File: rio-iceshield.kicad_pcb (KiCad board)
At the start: 2 copper layers, 87.6 x 56 mm, 71 parts, among them J2 Conn_01x06, J3 Conn_01x06, J4 Conn_01x06, J5 Conn_01x06, J6 Conn_01x06, J7 Conn_02x06_Odd_Even, U1 ICE40UP5K-SG48ITR, U10 PC817, U11 PC817, U12 PC817, U13 PC817, U14 PC817, U2 AT25SF081-SSHF-X, U3 LD3985M122R_SOT23, U4 ULN2803A, U5 ULN2803A, U7 PC817, U8 PC817, U9 PC817, X2 XO91, j1 GPIO

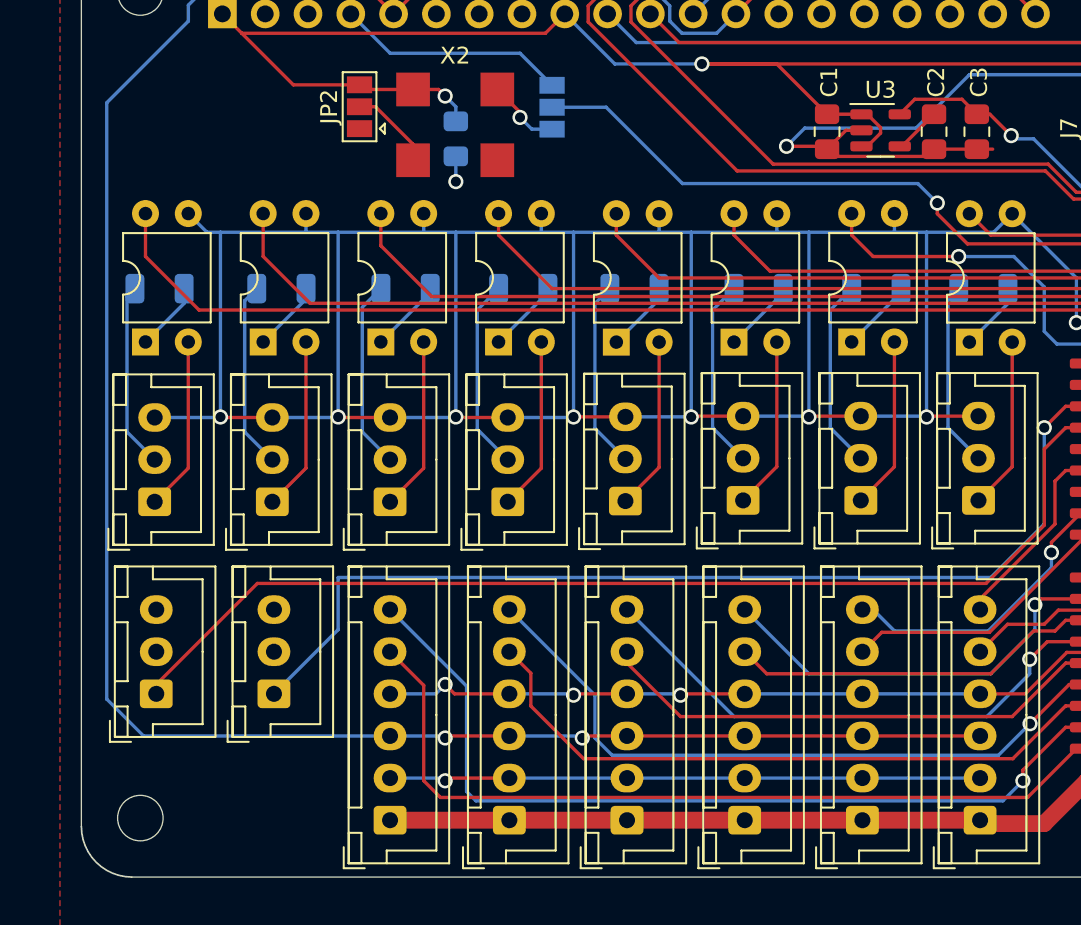
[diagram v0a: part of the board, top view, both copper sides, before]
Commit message: adding missing in/out powerlines
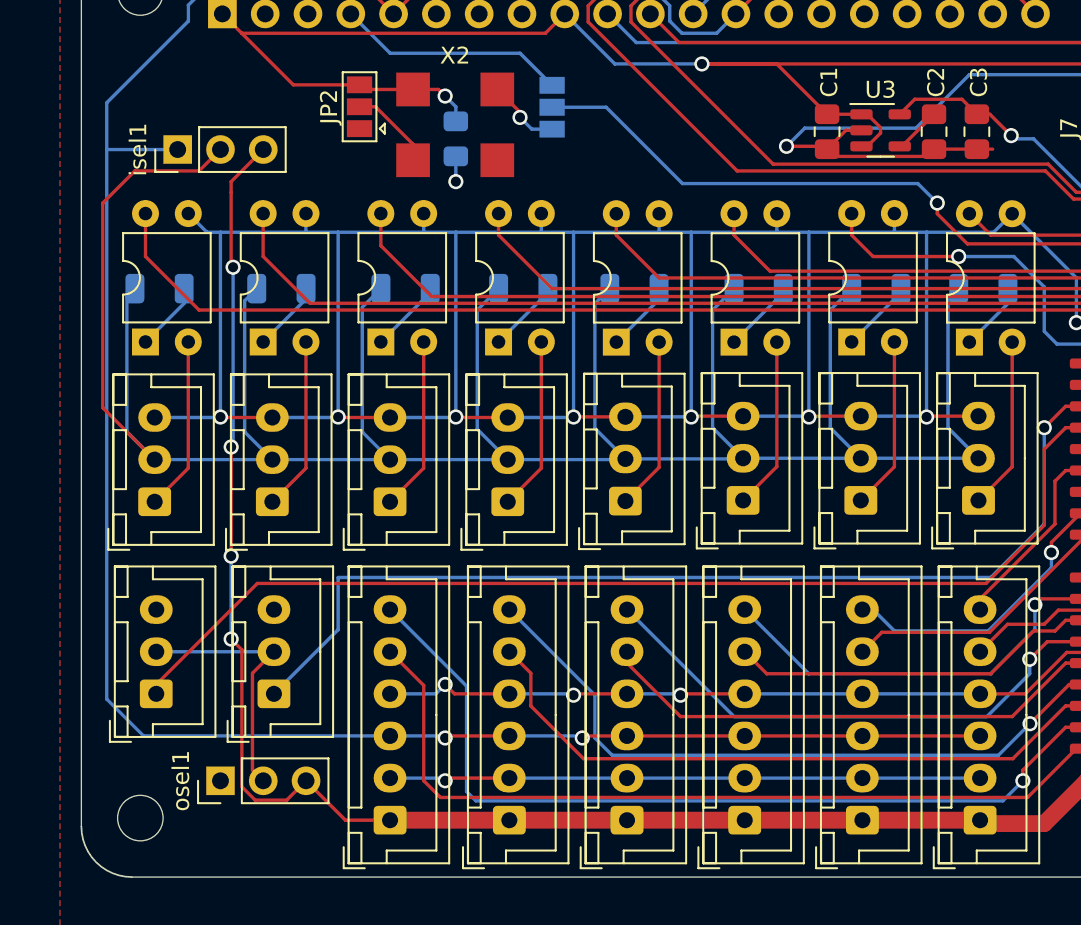
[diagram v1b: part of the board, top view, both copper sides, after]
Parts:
- added isel1: 5V 24V, Connector_PinHeader_2.54mm:PinHeader_1x03_P2.54mm_Vertical, F.Cu at (105.7, 56.8)
- added osel1: 5V 24V, Connector_PinHeader_2.54mm:PinHeader_1x03_P2.54mm_Vertical, F.Cu at (108.3, 94.3)
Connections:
- R2 pad 2: /input1/power -> in_power
- R3 pad 2: /input2/power -> in_power
- R4 pad 2: /input3/power -> in_power
- R5 pad 2: /input4/power -> in_power
- R6 pad 2: /input5/power -> in_power
- R7 pad 2: /input6/power -> in_power
- R8 pad 2: /input7/power -> in_power
- R9 pad 2: /input8/power -> in_power
- input1 pad 2: /input1/power -> in_power
- input2 pad 2: /input2/power -> in_power
- input3 pad 2: /input3/power -> in_power
- input4 pad 2: /input4/power -> in_power
- input5 pad 2: /input5/power -> in_power
- input6 pad 2: /input6/power -> in_power
- input7 pad 2: /input7/power -> in_power
- input8 pad 2: /input8/power -> in_power
- output1 pad 2: unconnected-(output1-Pin_2-Pad2) -> out_power
- output1 pad 3: unconnected-(output1-Pin_3-Pad3) -> gnd
- output2 pad 2: unconnected-(output2-Pin_2-Pad2) -> out_power
- output2 pad 3: unconnected-(output2-Pin_3-Pad3) -> gnd
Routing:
- net in_power: track 0.00 -> 163.6 mm
- net 12v: track 58.3 -> 108.1 mm, vias 0 -> 4
- net out_power: track 0.00 -> 15.4 mm
- net /input4/power: track 11.4 -> 0.00 mm
- net /input7/power: track 11.3 -> 0.00 mm
- net /input6/power: track 11.3 -> 0.00 mm
- net /input3/power: track 11.3 -> 0.00 mm
- net /input5/power: track 11.2 -> 0.00 mm
- net /input2/power: track 11.1 -> 0.00 mm
- net /input8/power: track 11.1 -> 0.00 mm
- net /input1/power: track 11.0 -> 0.00 mm
- net 5v: track 101.5 -> 105.7 mm

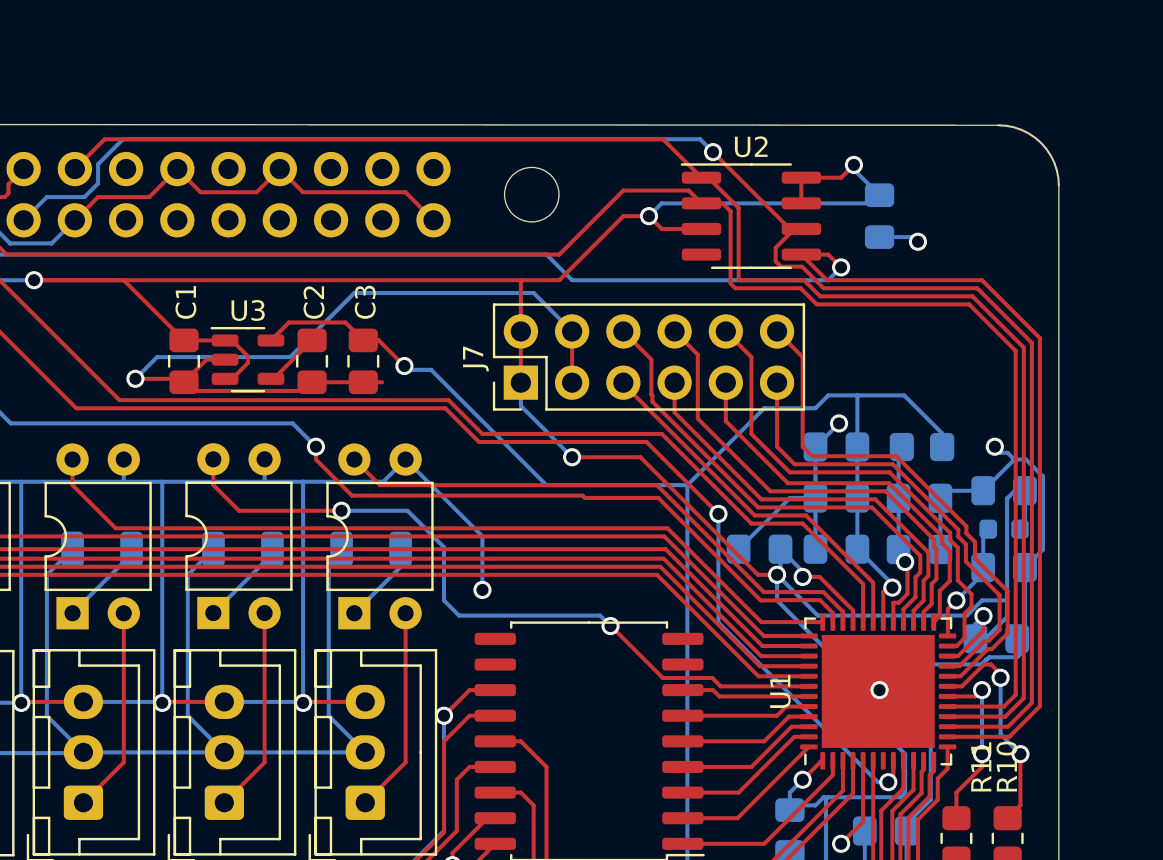
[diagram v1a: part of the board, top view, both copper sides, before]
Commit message: replacing spi-flash package
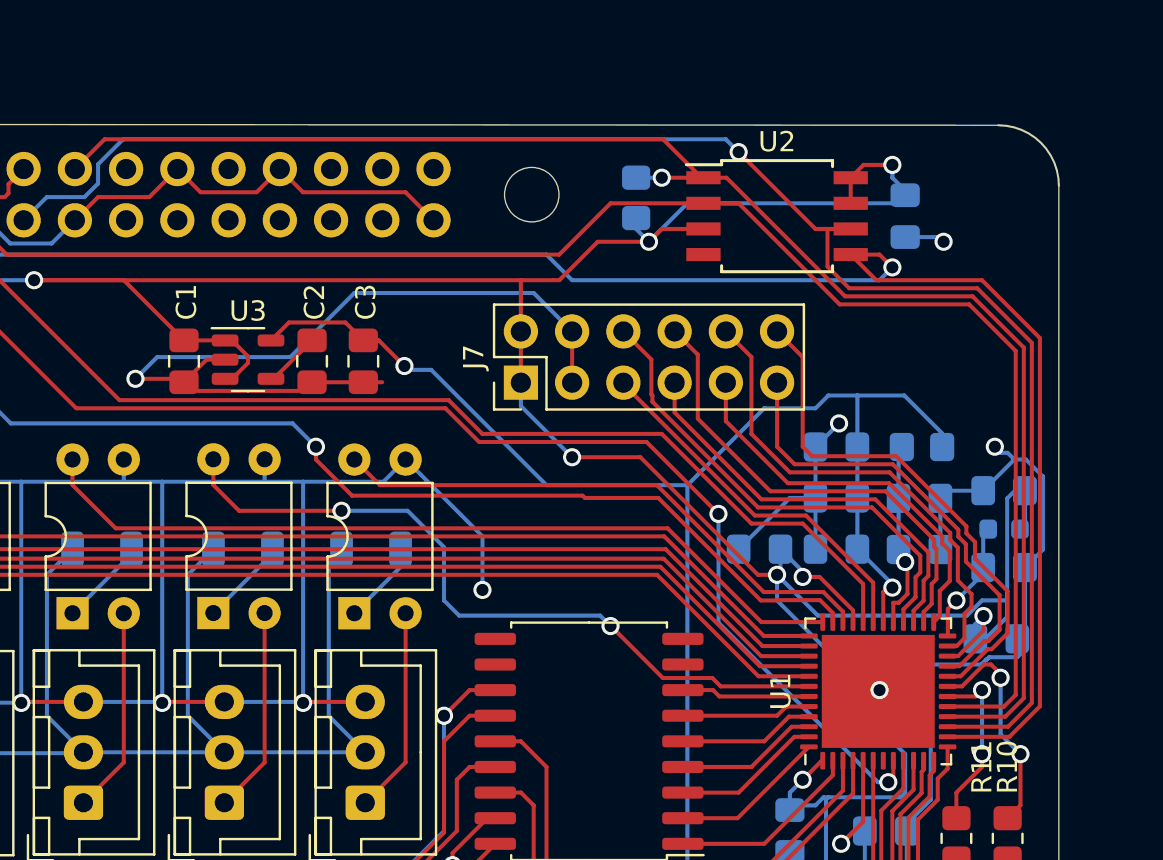
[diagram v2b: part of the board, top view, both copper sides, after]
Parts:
- added R12: 10k, Resistor_SMD:R_0805_2012Metric_Pad1.20x1.40mm_HandSolder, B.Cu at (166.7, 47.7)
- D1: value CDBU40-HF -> CDBU40-HF 800mV
- U2: value AT25SF081-SSHF-X -> AT25SF041B-SHD 4 Mb; footprint Package_SO:SOIC-8_3.9x4.9mm_P1.27mm -> Package_SO:SOIC-8W_5.3x5.3mm_P1.27mm
- isel1, osel1: value 5V 24V -> Conn_01x03
- moved U2 1.27 mm to (173.7, 48.6)
- moved C4 1.27 mm to (180.0, 48.6)
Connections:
- net Net-(D1-K) renamed 2v5
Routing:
- net SPI_MISO: track 79.8 -> 77.2 mm
- net 3v3: track 211.4 -> 213.3 mm
- net SPI_CS1: track 75.6 -> 76.7 mm, vias 0 -> 1
- net SPI_SCK: track 81.8 -> 81.2 mm

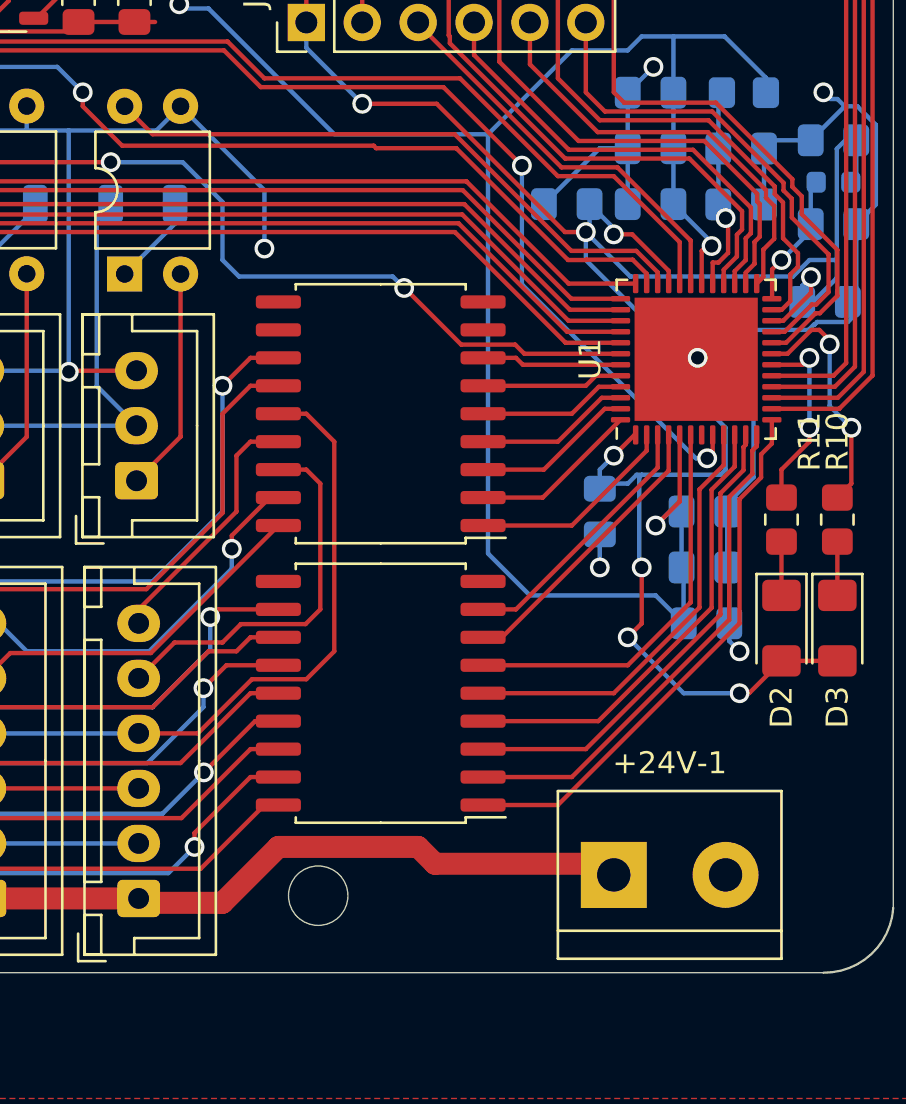
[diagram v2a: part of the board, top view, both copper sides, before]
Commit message: adding pulldowns to outputs / fixing uln gnd's
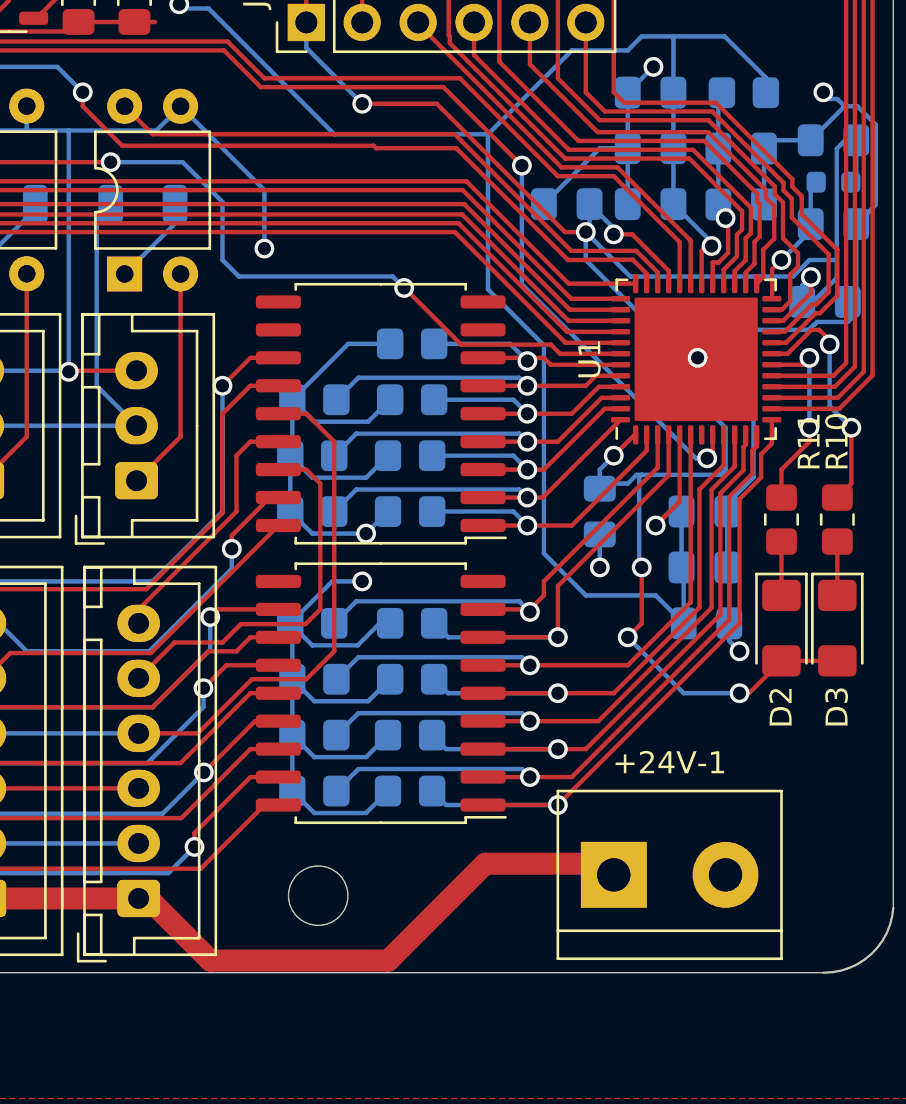
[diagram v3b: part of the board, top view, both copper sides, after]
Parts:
- added R13: 20k, Resistor_SMD:R_0805_2012Metric_Pad1.20x1.40mm_HandSolder, B.Cu at (165.7, 91.7)
- added R14: 20k, Resistor_SMD:R_0805_2012Metric_Pad1.20x1.40mm_HandSolder, B.Cu at (161.3, 91.7)
- added R15: 20k, Resistor_SMD:R_0805_2012Metric_Pad1.20x1.40mm_HandSolder, B.Cu at (165.7, 89.2)
- added R16: 20k, Resistor_SMD:R_0805_2012Metric_Pad1.20x1.40mm_HandSolder, B.Cu at (161.3, 89.2)
- added R17: 20k, Resistor_SMD:R_0805_2012Metric_Pad1.20x1.40mm_HandSolder, B.Cu at (165.8, 86.7)
- added R18: 20k, Resistor_SMD:R_0805_2012Metric_Pad1.20x1.40mm_HandSolder, B.Cu at (161.3, 86.7)
- added R19: 20k, Resistor_SMD:R_0805_2012Metric_Pad1.20x1.40mm_HandSolder, B.Cu at (165.8, 84.1)
- added R20: 20k, Resistor_SMD:R_0805_2012Metric_Pad1.20x1.40mm_HandSolder, B.Cu at (161.2, 84.1)
- added R21: 20k, Resistor_SMD:R_0805_2012Metric_Pad1.20x1.40mm_HandSolder, B.Cu at (165.7, 79.0)
- added R22: 20k, Resistor_SMD:R_0805_2012Metric_Pad1.20x1.40mm_HandSolder, B.Cu at (161.2, 79.0)
- added R23: 20k, Resistor_SMD:R_0805_2012Metric_Pad1.20x1.40mm_HandSolder, B.Cu at (165.7, 76.5)
- added R24: 20k, Resistor_SMD:R_0805_2012Metric_Pad1.20x1.40mm_HandSolder, B.Cu at (161.2, 76.5)
- added R25: 20k, Resistor_SMD:R_0805_2012Metric_Pad1.20x1.40mm_HandSolder, B.Cu at (165.8, 74.0)
- added R26: 20k, Resistor_SMD:R_0805_2012Metric_Pad1.20x1.40mm_HandSolder, B.Cu at (161.3, 74.0)
- added R27: 20k, Resistor_SMD:R_0805_2012Metric_Pad1.20x1.40mm_HandSolder, B.Cu at (165.8, 71.4)
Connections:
- U4 pad 9: unconnected-(U4-GND-Pad9) -> gnd
- U5 pad 9: unconnected-(U5-GND-Pad9) -> gnd
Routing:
- net gnd: track 378.4 -> 437.6 mm, vias 17 -> 19
- net 3: track 12.1 -> 22.0 mm, vias 0 -> 1
- net 6: track 18.2 -> 27.6 mm, vias 0 -> 1
- net 10: track 20.8 -> 30.2 mm, vias 0 -> 1
- net 12: track 23.1 -> 32.4 mm, vias 0 -> 1
- net 46: track 7.07 -> 16.4 mm, vias 0 -> 1
- net 48: track 7.71 -> 17.1 mm, vias 0 -> 1
- net 44: track 6.44 -> 15.7 mm, vias 0 -> 1
- net 4: track 13.2 -> 20.6 mm, vias 0 -> 1
- net 11: track 22.0 -> 27.9 mm, vias 0 -> 1
- net 13: track 24.9 -> 30.9 mm, vias 0 -> 1
- net 9: track 19.7 -> 25.6 mm, vias 0 -> 1
- net 47: track 7.39 -> 12.0 mm, vias 0 -> 1
- net 2: track 9.56 -> 14.2 mm, vias 0 -> 1
- net 43: track 6.38 -> 10.9 mm, vias 0 -> 1
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
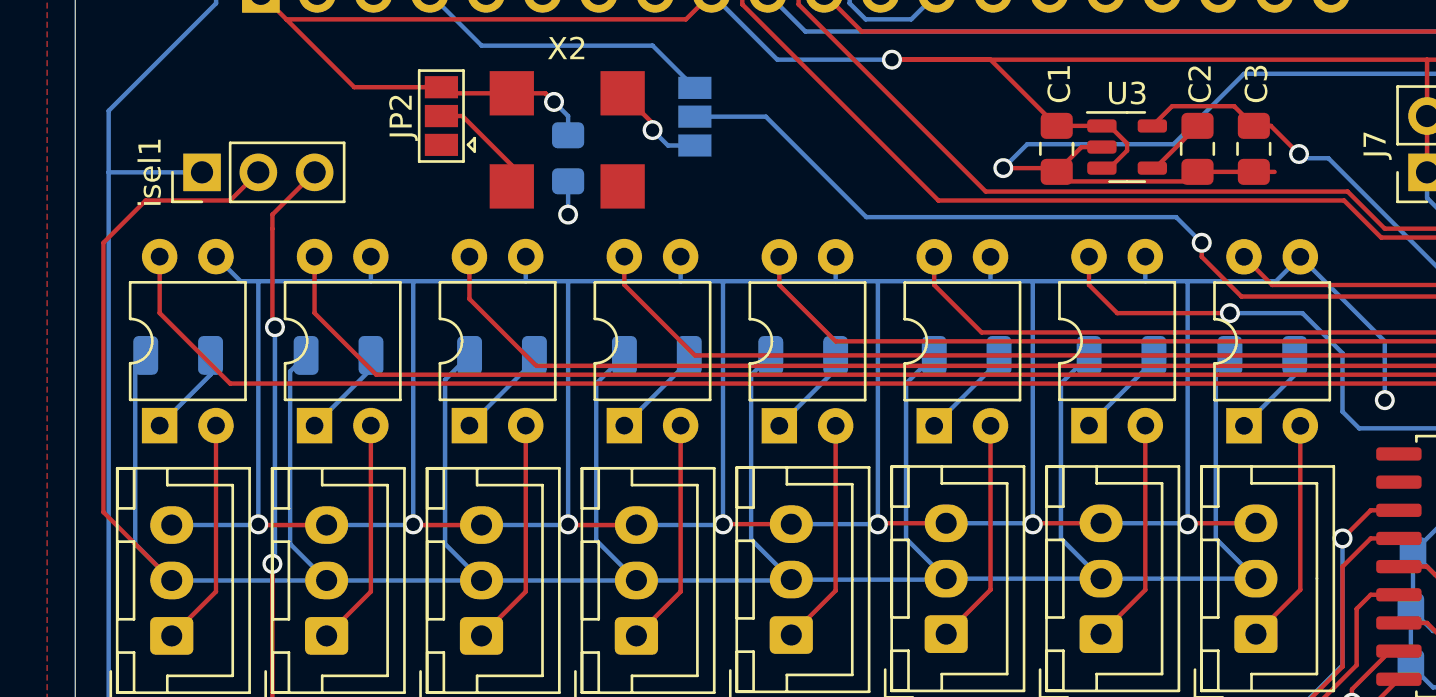
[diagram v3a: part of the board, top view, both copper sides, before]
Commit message: adding pullups to in1-3
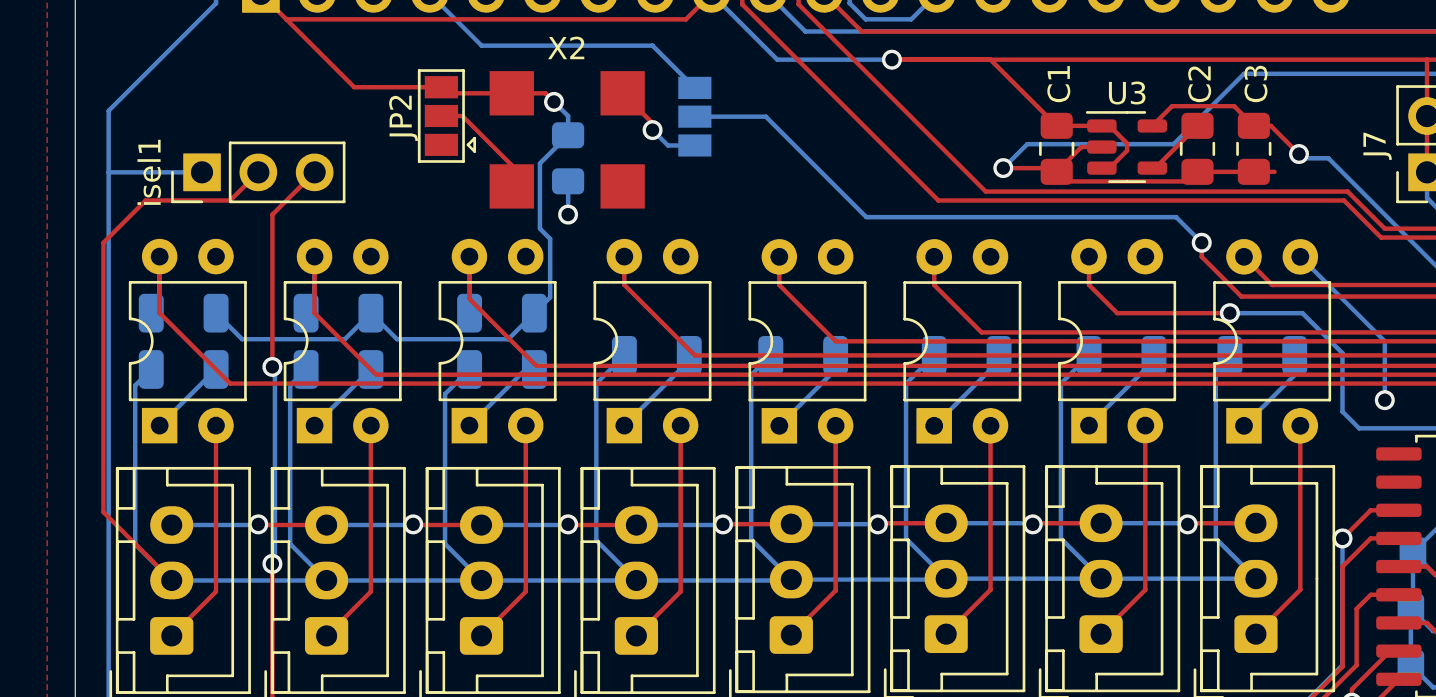
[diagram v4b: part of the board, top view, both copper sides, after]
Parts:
- added R28: 20K, Resistor_SMD:R_1206_3216Metric, B.Cu at (119.2, 63.2)
- added R29: 20K, Resistor_SMD:R_1206_3216Metric, B.Cu at (111.9, 63.2)
- added R30: 20K, Resistor_SMD:R_1206_3216Metric, B.Cu at (104.9, 63.2)
- D1: value CDBU40-HF 800mV -> 1N 4148WT7 DII
- R2, R3, R4, R5, R6, R7, R8, R9: value R -> 3K3
- moved R2 0.68 mm to (104.9, 65.7)
- moved R3 0.63 mm to (111.9, 65.7)
- moved R4 0.63 mm to (119.2, 65.7)
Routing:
- net gnd: track 437.6 -> 304.3 mm
- net 3v3: track 213.3 -> 238.6 mm
- net 41: track 77.4 -> 80.1 mm
- net 40: track 70.2 -> 72.9 mm
- net 39: track 62.6 -> 65.2 mm
- net in_power: track 163.6 -> 161.8 mm
- net Net-(R3-Pad1): track 4.22 -> 3.60 mm
- net Net-(R2-Pad1): track 4.12 -> 3.59 mm
